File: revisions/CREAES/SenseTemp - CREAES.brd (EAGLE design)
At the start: 61 x 22.9 mm, 46 parts, among them Q1 mmbt2222, U1 MIC5225-3.3, U2 AT21CS01, U3 MAX31865, U4 MAX31865, U5 MAX31865, U6 MAX31865

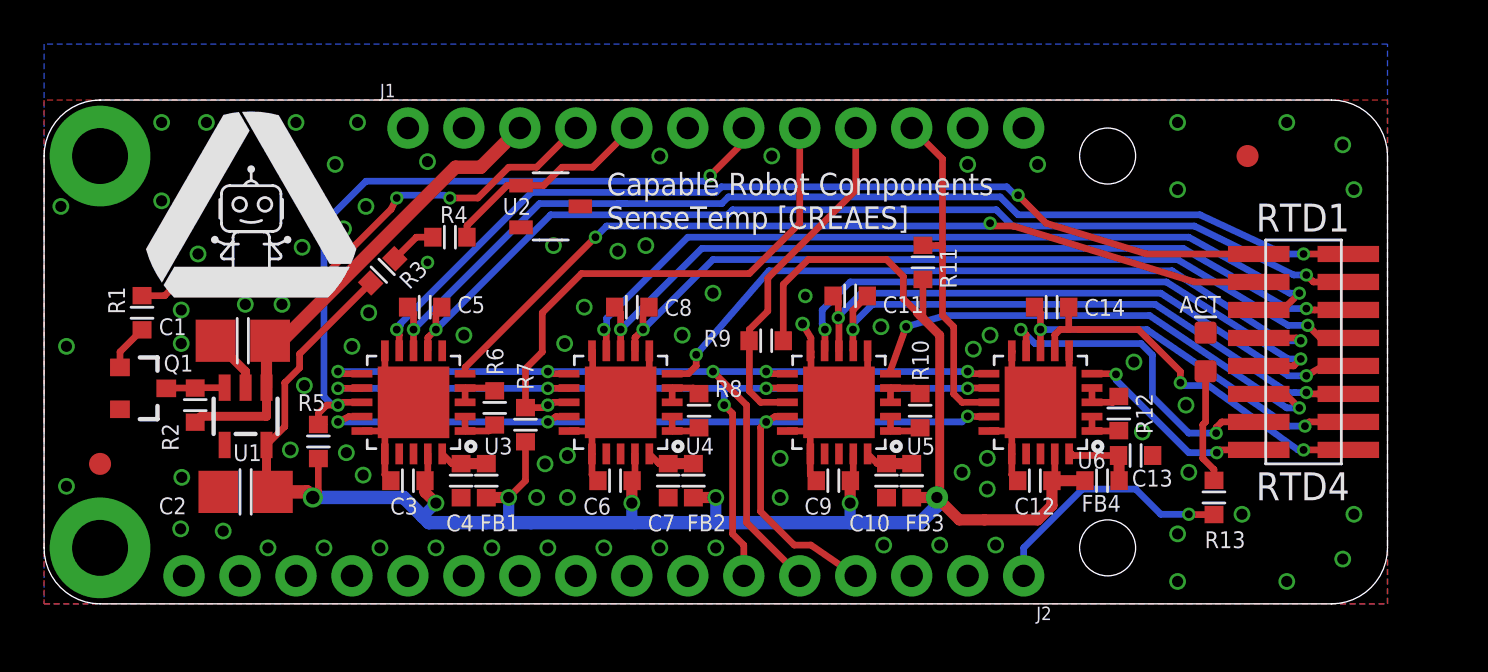
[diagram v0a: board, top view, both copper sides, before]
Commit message: Change silk screen around RTD connector
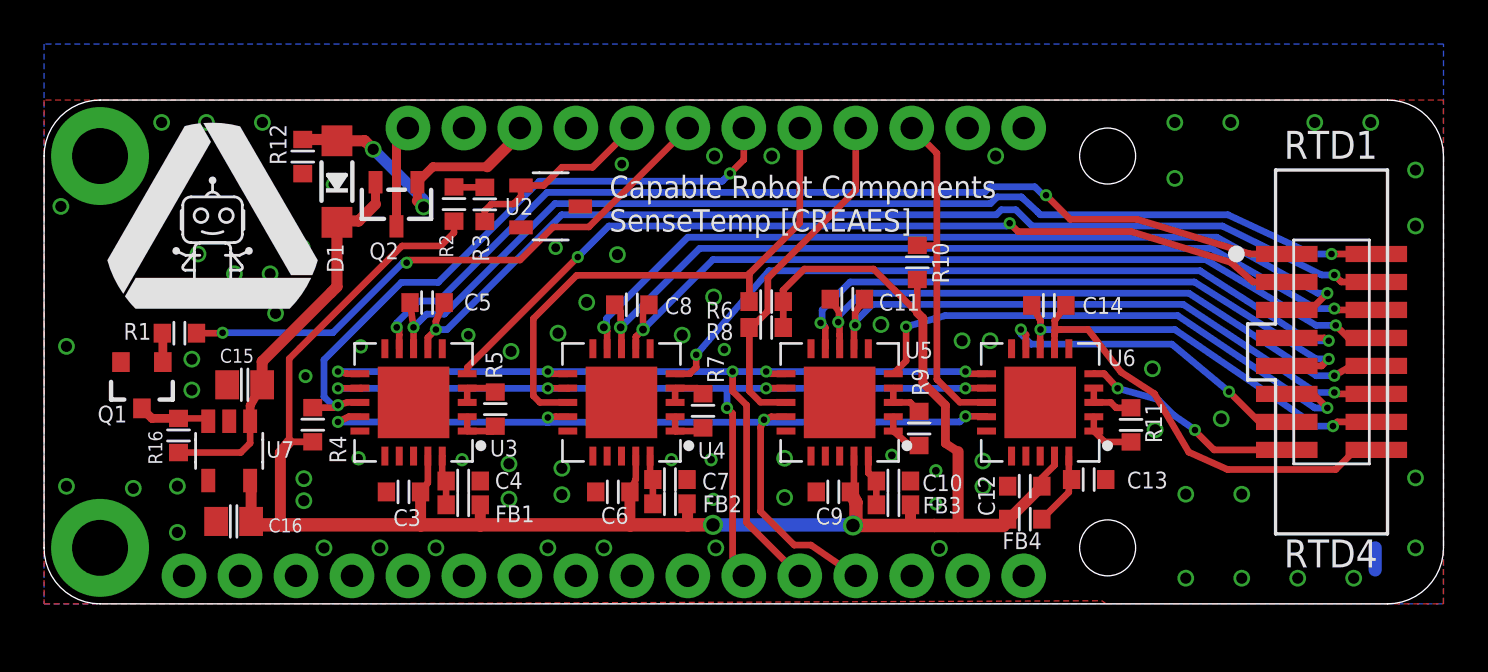
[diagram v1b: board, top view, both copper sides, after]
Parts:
- removed ACT: (no value), SparkFun-LED:LED-0603
- removed C1, C2: 10u, CapableRobot:1206
- removed FID1, FID2: FIDUCIAL"", microbuilder:FIDUCIAL_1MM
- removed J1: (no value), SparkFun-Connectors:1X12_NO_SILK
- removed J2: (no value), SparkFun-Connectors:1X16_NO_SILK
- removed R13: 1k, CapableRobot:0603
- removed U1: MIC5225-3.3, microbuilder:SOT23-5
- added C15, C16: 10u, CapableRobot:0805
- added D1: MBR120, Adafruit Feather M0 Express:SOD-123
- added J3: FEATHERPTH, CapableRobot:FEATHER-PTH
- added Q2: DMP2045, Adafruit Feather M4 Express:SOT23-R
- added R16: 10k, CapableRobot:0603
- added U7: 3v3, CapableRobot:SOT25
- LOGO1: value CRC-LOGO10 -> CRC-LOGO7SILK; device CapableRobot:CRC-LOGO-10 -> CapableRobot:CRC-LOGO-7-SILK
- Q1: value mmbt2222 -> MMBT2222; device SparkFun-DiscreteSemi:SOT23-3 -> Adafruit HUZZAH32 ESP32 Feather:SOT23-3
- R10, R6, R8: value 4K3 0.1% -> 10k
- R11, R5, R7, R9: value 10k -> 4k3 0.05%
- R12: value 4K3 0.1% -> 100k
- R2: value 10k -> 1k
- R4: value 1k -> 10k
- U3, U4, U5, U6: device microbuilder:QFN20_4MM_0.65MM -> CapableRobot:QFN65P500X500X100-21T325
- moved R12 38.8 mm to (11.7, 20.3)
- moved R2 14.9 mm to (18.6, 18.1)
- moved R6 13.2 mm to (32.8, 13.7), turned to 0 degrees
- moved R11 12.0 mm to (49.3, 8.12)
- moved R4 10.5 mm to (12.2, 8.13), turned to 270 degrees
- moved R5 8.16 mm to (20.5, 8.84)
- moved R7 8.08 mm to (29.9, 8.76)
- moved R9 8.00 mm to (39.7, 7.96), turned to 270 degrees
- moved R10 6.73 mm to (39.6, 15.5), turned to 270 degrees
- moved R3 5.52 mm to (20.0, 18.1), turned to 90 degrees
- moved R8 4.85 mm to (32.8, 12.5), turned to 0 degrees
- moved FB4 3.92 mm to (44.5, 3.84)
- moved C13 2.39 mm to (47.4, 5.64), turned to 0 degrees
- moved R1 1.93 mm to (6.14, 12.3), turned to 180 degrees
- moved LOGO2 1.82 mm to (7.65, 16.9)
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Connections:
- removed net +5V: C1.P$2, J1.3, R2.2, U1.1
- removed net LED: J2.1, R13.1
- removed net N$17 (its old number): R3.1, R4.2
- removed net N$18: ACT.A, R13.2
- removed net N$3: Q1.3, R2.1, U1.3
- new net EN: Q1.3, R16.2, U7.3
- new net N$4: R2.1, R3.2
- new net VBAT: J3.BAT, Q2.3
- new net VBUS: D1.A, J3.USB, Q2.1, R12.2
- new net VIN: C15.2, D1.C, Q2.2, R16.1, U7.1
- net !EN: now also J3.5; no longer J1.4
- net +3V3: now also C12.1, C16.2, C3.1, C6.1, C9.1, R10.2, R2.2, R4.2, R6.2, R8.2, U7.5; no longer C12.2, C2.P$2, C3.2, C6.2, C9.2, R11.2, R3.2, R5.2, R7.2, R9.2, U1.5
- net CS1: now also J3.4, R4.1; no longer J1.7, R5.1
- net CS2: now also J3.3, R6.1; no longer J1.8, R7.1
- net CS3: now also J3.2, R8.1; no longer J1.9, R9.1
- net CS4: now also J3.1, R10.1; no longer J1.10, R11.1
- net GND: now also C10.2, C12.2, C13.2, C15.1, C16.1, C3.2, C4.2, C6.2, C7.2, C9.2, J3.GND, R12.1, U3.21, U4.21, U5.21, U6.21, U7.2; no longer ACT.C, C1.P$1, C10.1, C12.1, C13.1, C2.P$1, C3.1, C4.1, C6.1, C7.1, C9.1, J2.13, U1.2, U3.PAD, U4.PAD, U5.PAD, U6.PAD
- net MISO: now also J3.MISO; no longer J2.4
- net MOSI: now also J3.MOSI; no longer J2.5
- net N$10: now also C7.1; no longer C7.2
- net N$11: now also R9.2; no longer R10.1
- net N$12: now also R9.1; no longer R10.2
- net N$13: now also C10.1; no longer C10.2
- net N$14: now also R11.2; no longer R12.1
- net N$15: now also R11.1; no longer R12.2
- net N$16: now also C13.1; no longer C13.2
- net N$5: now also R5.2; no longer R6.1
- net N$6: now also R5.1; no longer R6.2
- net N$7: now also C4.1; no longer C4.2
- net N$8: now also R7.2; no longer R8.2
- net N$9: now also R7.1; no longer R8.1
- net RTDIN1+: now also C5.1; no longer C5.2
- net RTDIN1-: now also C5.2; no longer C5.1
- net RTDIN2+: now also C8.1; no longer C8.2
- net RTDIN2-: now also C8.2; no longer C8.1
- net RTDIN3+: now also C11.1; no longer C11.2
- net RTDIN3-: now also C11.2; no longer C11.1
- net RTDIN4+: now also C14.1; no longer C14.2
- net RTDIN4-: now also C14.2; no longer C14.1
- net SCLK: now also J3.SCK; no longer J2.6
- net SIO: now also J3.6, R3.1; no longer J1.5, R4.1
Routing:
- net GND: track 44.0 -> 1.44 mm, vias 81 -> 79
- net +5V: track 22.2 -> 0.00 mm
- net VIN: track 0.00 -> 18.1 mm
- net VBUS: track 0.00 -> 14.0 mm, vias 0 -> 2
- net LED: track 11.5 -> 0.00 mm, vias 1 -> 0
- net N$18: track 5.22 -> 0.00 mm
- net VBAT: track 0.00 -> 4.68 mm
- net CS1: track 32.8 -> 28.9 mm
- net EN: track 0.00 -> 3.25 mm
- net !EN: track 23.0 -> 26.2 mm
- net N$3: track 2.66 -> 0.00 mm
- net N$17 (its old number): track 2.13 -> 0.00 mm
- net FORCE3-: track 27.2 -> 28.9 mm
- net FORCE1+: track 39.4 -> 40.9 mm
- net RTDIN2-: track 37.6 -> 39.0 mm
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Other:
- board size 61 x 22.9 mm -> 63.5 x 22.9 mm
- board text added: "5V"
- board text added: "EN"
- board text removed: "!EN"
- board text removed: "USR"
- board text removed: "VIN"
